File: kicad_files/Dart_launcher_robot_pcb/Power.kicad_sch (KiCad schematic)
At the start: 5 parts, among them J10 Conn_01x08_Pin, J22 Conn_01x02_Pin, J7 Conn_01x08_Pin, J8 Conn_01x08_Pin, J9 Conn_01x08_Pin

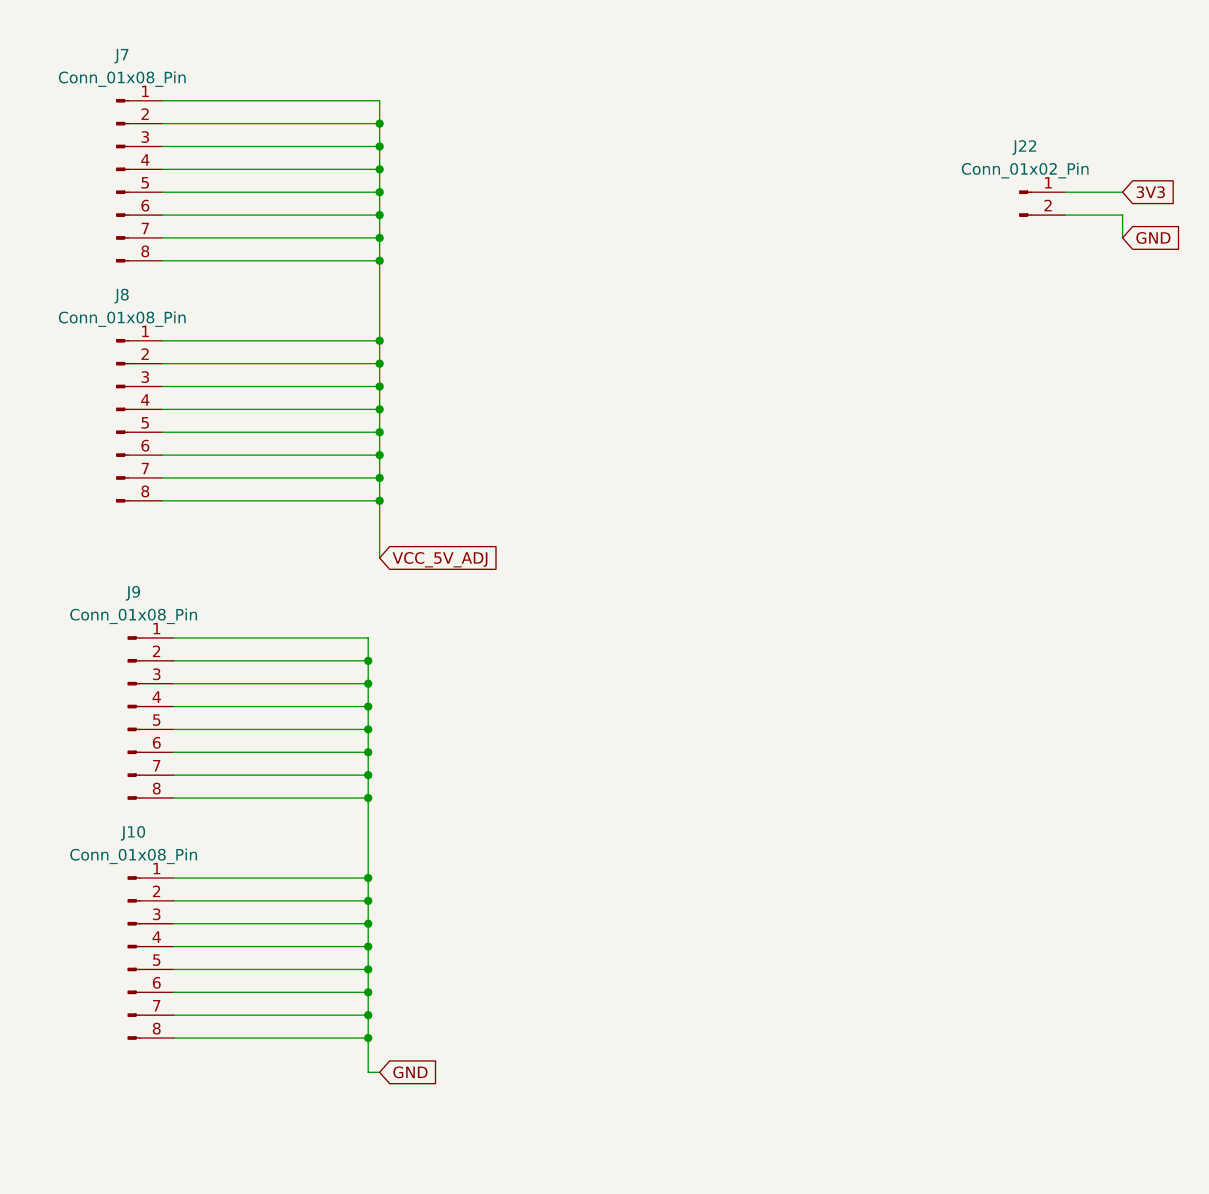
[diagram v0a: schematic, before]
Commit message: pcb design and changes to the pitch_yaw_launcher_code
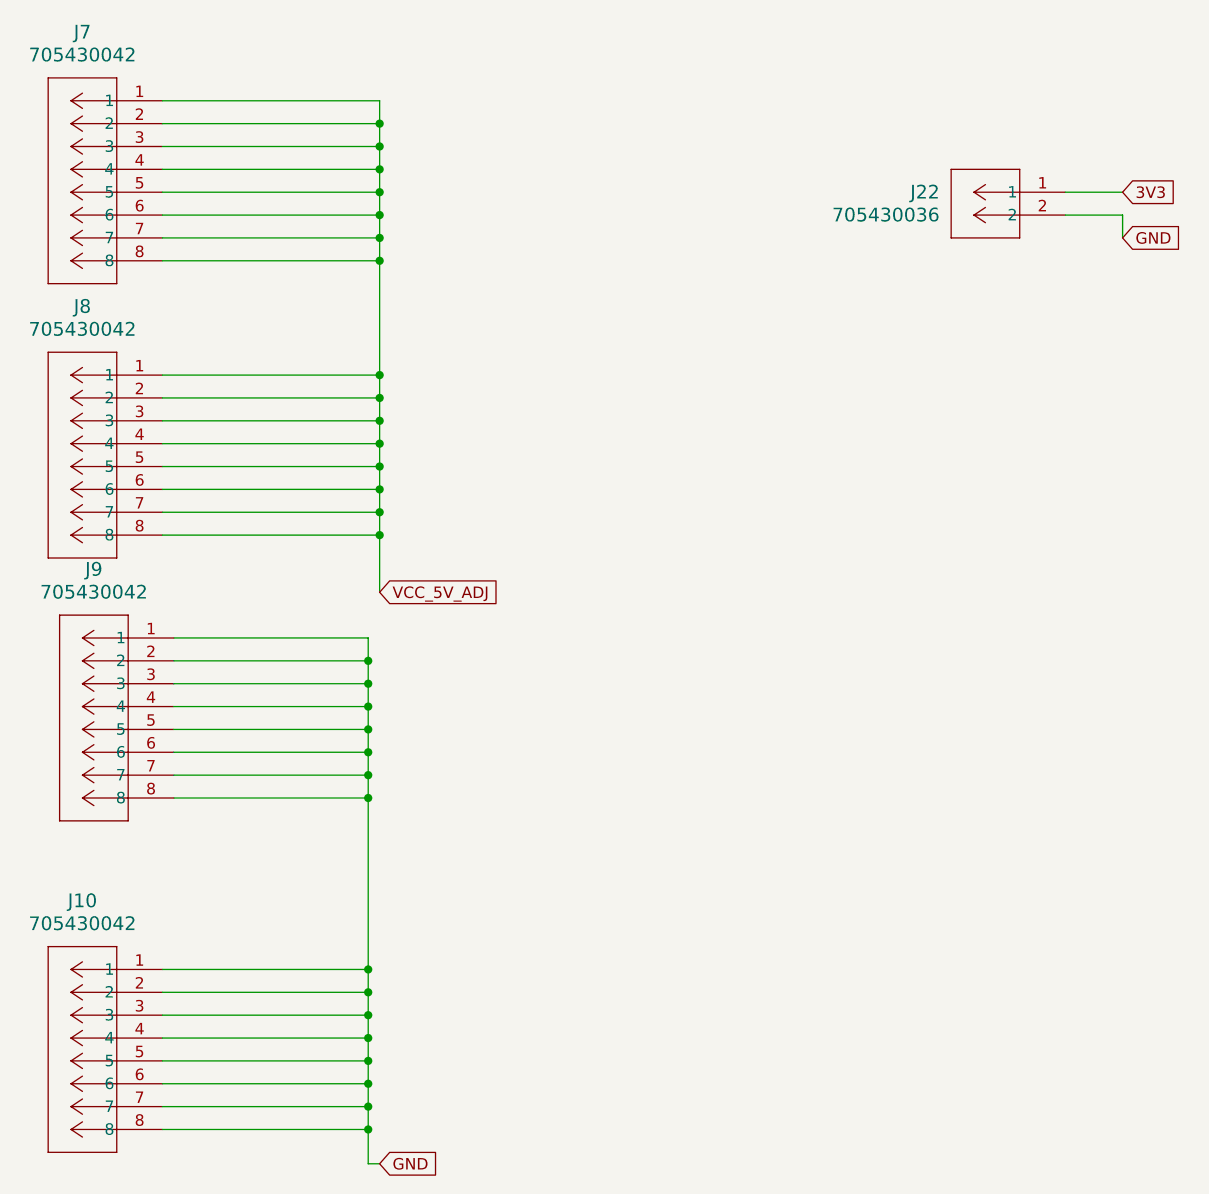
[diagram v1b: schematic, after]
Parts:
- removed J10, J7, J8, J9: Conn_01x08_Pin, Connector_PinHeader_2.54mm:PinHeader_1x08_P2.54mm_Vertical, symbol Connector:Conn_01x08_Pin
- removed J22: Conn_01x02_Pin, Connector_PinHeader_2.54mm:PinHeader_1x02_P2.54mm_Vertical, symbol Connector:Conn_01x02_Pin
- added J10, J7, J8, J9: 705430042, CONN_SDA-70543-xxxx_08_MOL, symbol Molex_705430042:705430042
- added J22: 705430036, CONN_SDA-70543-xxxx_02_MOL, symbol Molex_705430036:705430036
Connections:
- net 3V3: now also J22.1
- net GND: now also J10.1, J10.2, J10.3, J10.4, J10.5, J10.6, J10.7, J10.8, J22.2, J9.1, J9.2, J9.3, J9.4, J9.5, J9.6, J9.7, J9.8
- net VCC_5V_ADJ: now also J7.1, J7.2, J7.3, J7.4, J7.5, J7.6, J7.7, J7.8, J8.1, J8.2, J8.3, J8.4, J8.5, J8.6, J8.7, J8.8
